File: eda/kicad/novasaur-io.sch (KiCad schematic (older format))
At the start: 72 parts, among them J1 POWER IN, J3 AUDIO OUT, J4 KEYBOARD, J5 SERIAL, J5 SPKR, J6 DISPLAY, J7 EXPANSION, J8 EXP OUT, J9 VIDEO, Q4 BS270, SW1 POWER, U1 74F86, U2 74F08, U38 CD4053, U39 MAX232, U4 74F32, U40 NJM4580, U41 MCP1827S, U6 74F139, U7 74F139

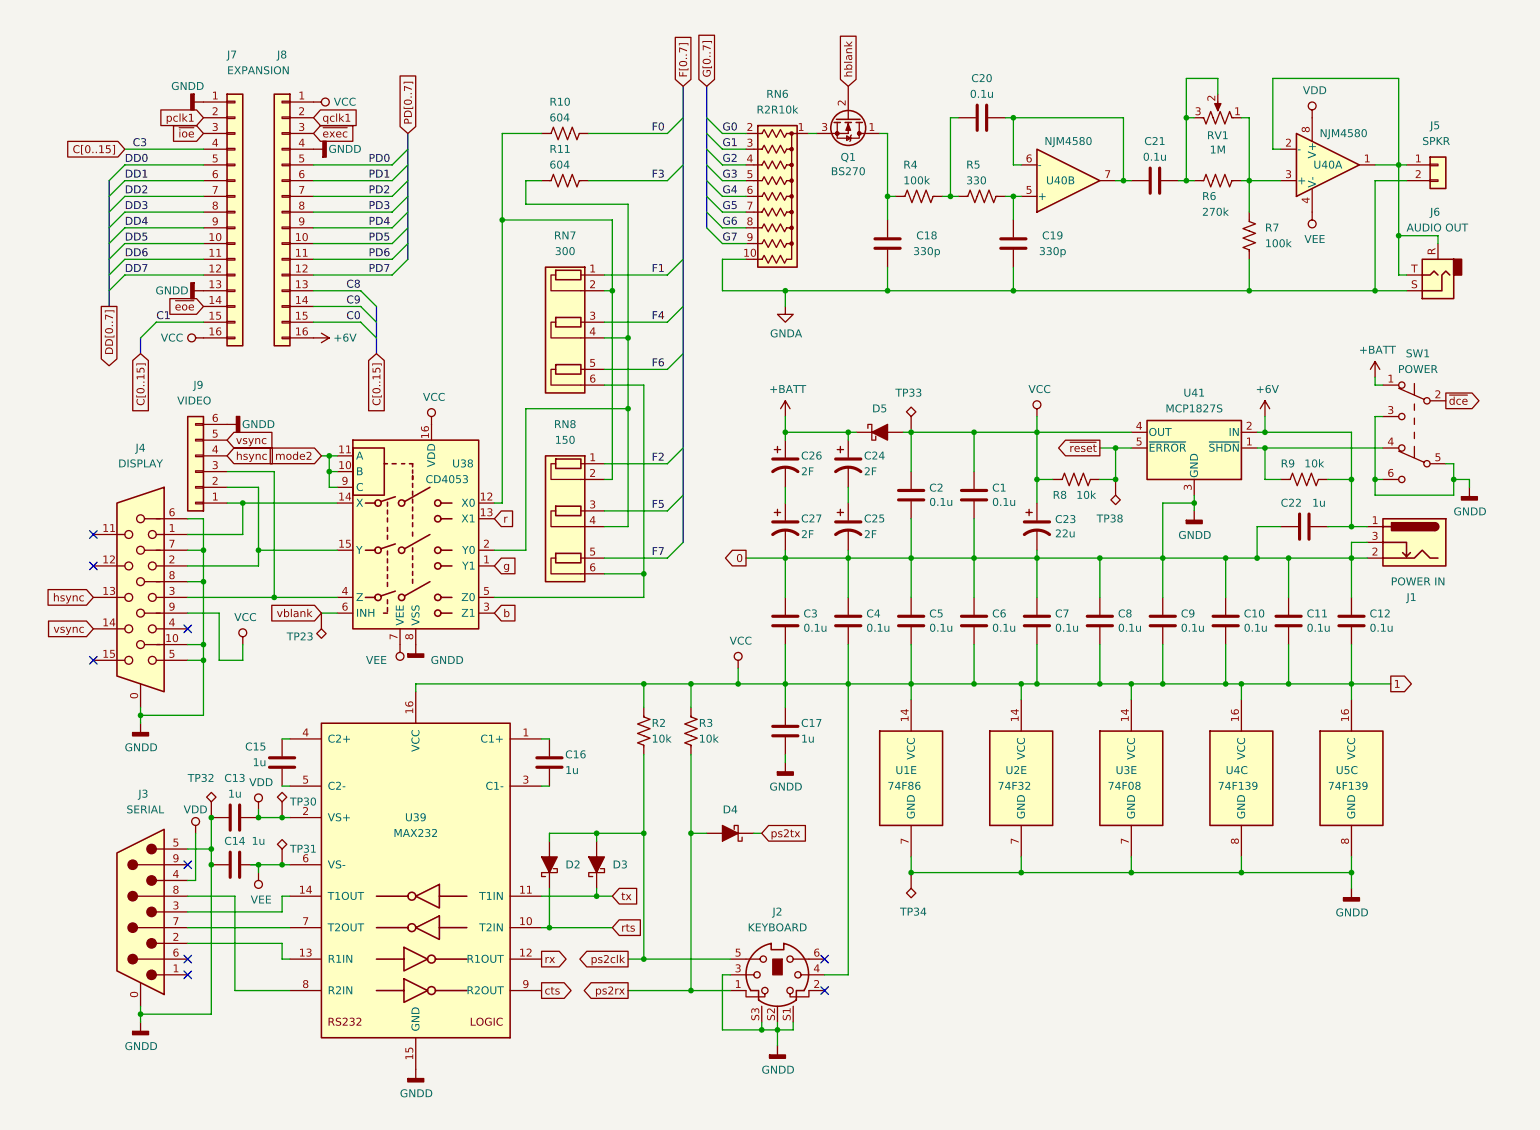
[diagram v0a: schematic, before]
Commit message: add dedicated ps2 clock enable line Use mode0|1 to select VDAC using DRL
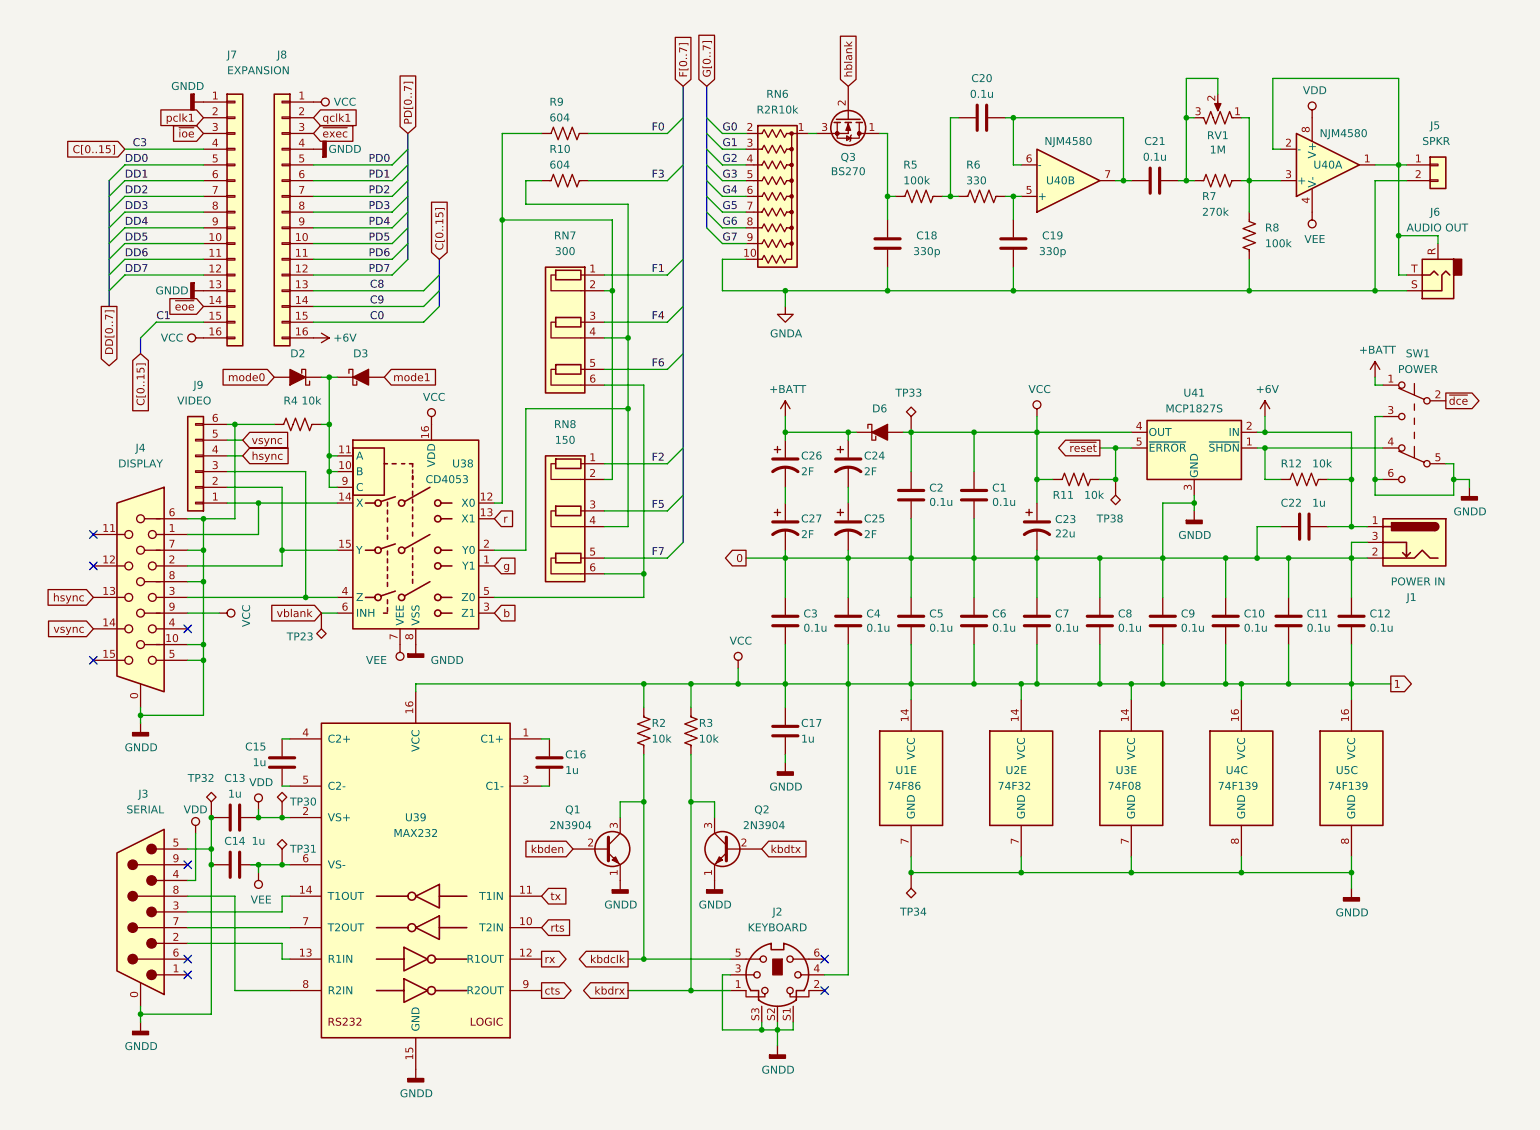
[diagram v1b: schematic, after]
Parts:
- removed D4: BAT42, Diode_THT:D_DO-35_SOD27_P7.62mm_Horizontal, symbol Device:D_Schottky_ALT
- added Q1, Q2: 2N3904, Package_TO_SOT_THT:TO-92_HandSolder, symbol Transistor_BJT:2N3904
- added R4: 10k, Resistor_THT:R_Axial_DIN0204_L3.6mm_D1.6mm_P7.62mm_Horizontal, symbol Device:R_US
- renumbered D5 to D6, R11 to R10, R8 to R11, R9 to R12, R4 to R5, R5 to R6, R6 to R7, R7 to R8, R10 to R9
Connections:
- net GNDD: now also Q1.1 (E), Q2.1 (E), R4.1
- net rts: no longer D2.1 (K)
- net tx: no longer D3.1 (K)
- net mode2: no longer names the net of U38.10 (B), U38.11 (A), U38.9 (C)
- net mode2: now also D2.1 (K), D3.1 (K), R4.2
- net ps2clk renamed kbdclk
- net kbdclk: now also Q1.3 (C); no longer D2.2 (A), D3.2 (A)
- net ps2rx renamed kbdrx
- net kbdrx: now also Q2.3 (C)
- new net kbden: Q1.2 (B)
- new net kbdtx: Q2.2 (B)
- new net mode0: D2.2 (A)
- new net mode1: D3.2 (A)

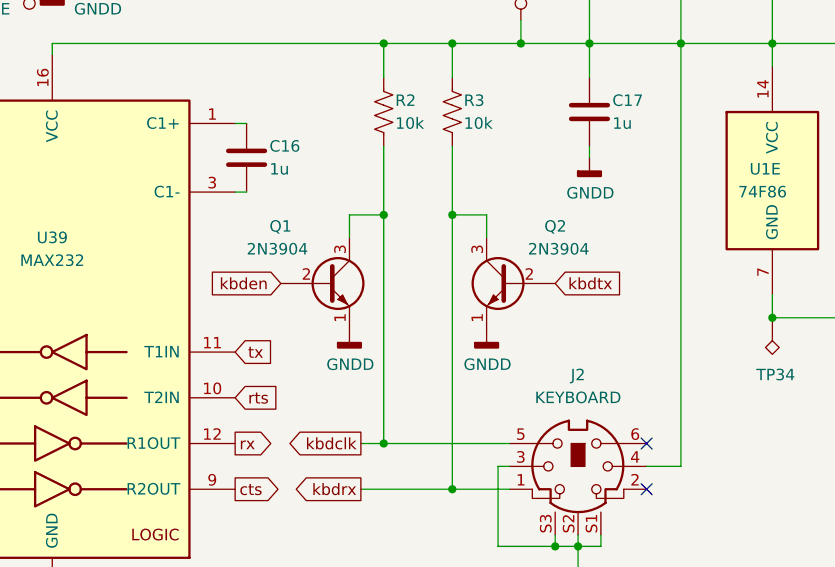
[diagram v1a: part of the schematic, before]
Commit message: refactor comms Add keyboard scan jump page, overload tx mode state to select keyboard jump page
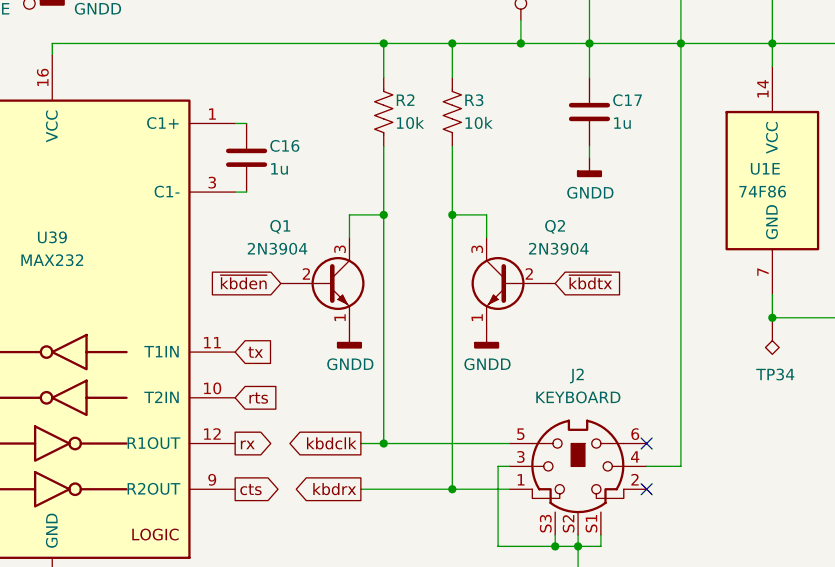
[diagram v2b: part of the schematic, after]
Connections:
- net kbden renamed ~kbden
- net kbdtx renamed ~kbdtx
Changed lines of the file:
@@
 	5300 7100 5400 7100
 Text GLabel 5300 5950 2    50   Input ~ 0
-kbdtx
+~kbdtx
 Connection ~ 5150 4900
 Connection ~ 5300 7100
@@
 $EndComp
 Text GLabel 4100 5950 0    50   Input ~ 0
-kbden
+~kbden
 $Comp
 L Device:R_US R?

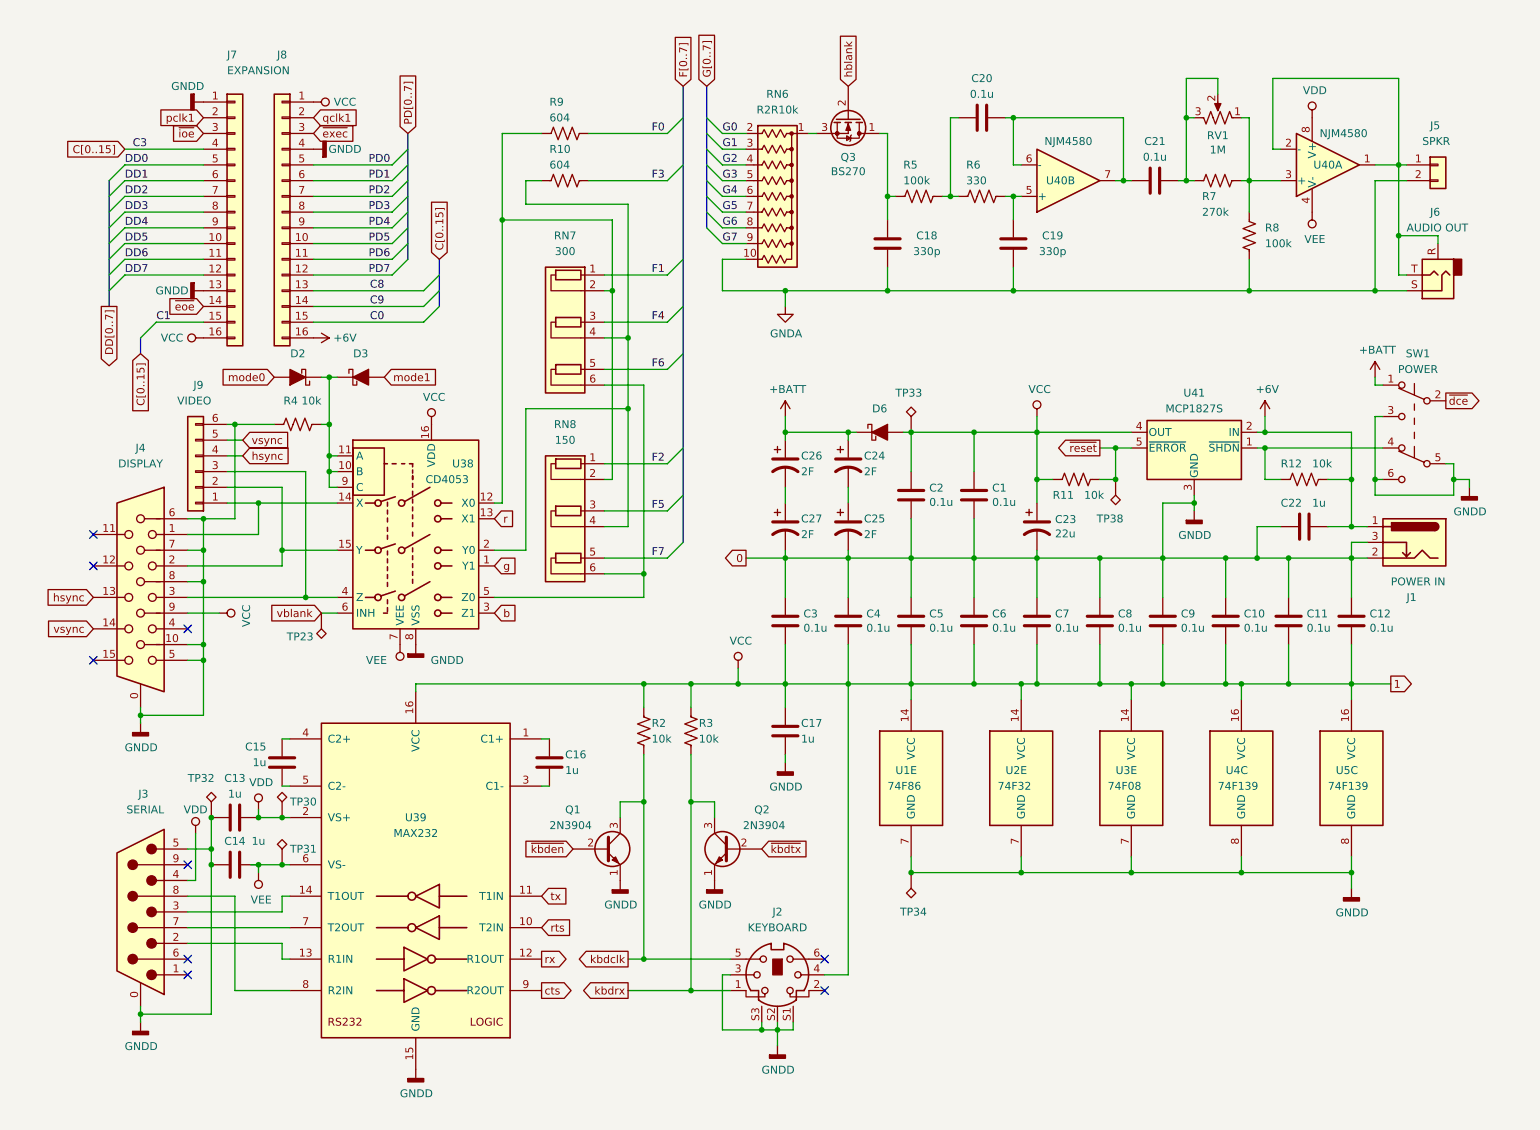
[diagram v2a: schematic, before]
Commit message: fix video timing debug and finish video modes
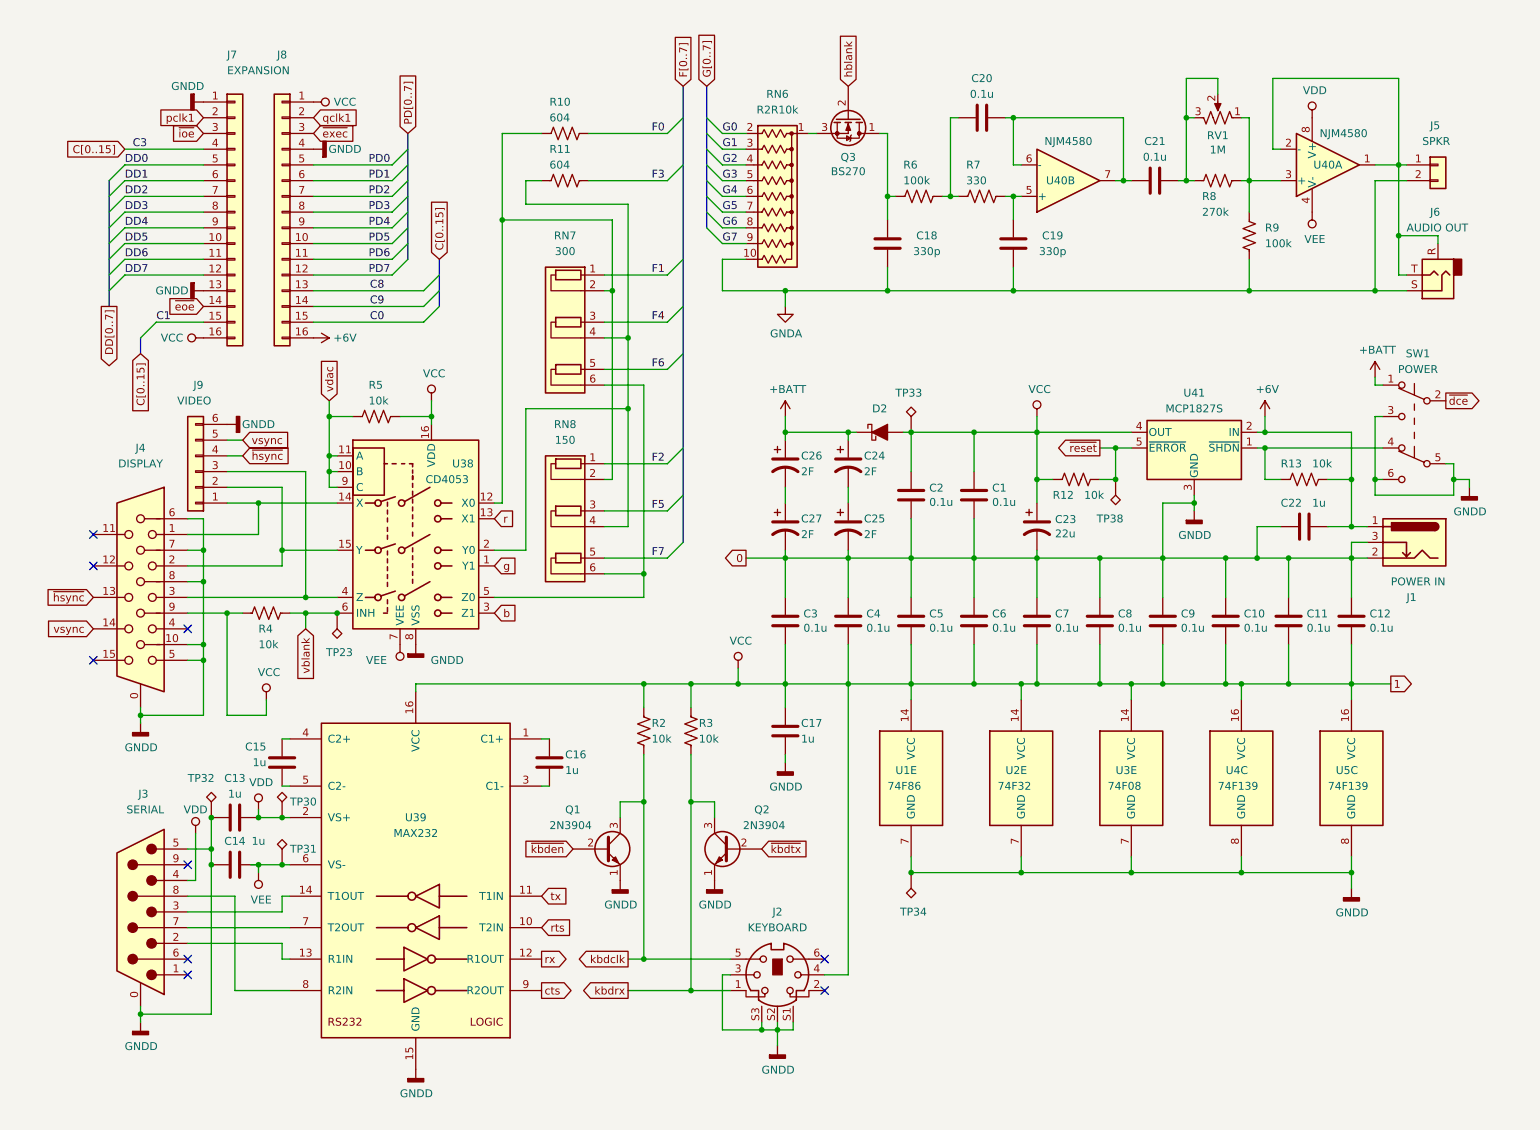
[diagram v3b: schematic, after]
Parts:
- removed D2, D3: BAT42, Diode_THT:D_DO-35_SOD27_P7.62mm_Horizontal, symbol Device:D_Schottky_ALT
- added R5: 10k, Resistor_THT:R_Axial_DIN0204_L3.6mm_D1.6mm_P7.62mm_Horizontal, symbol Device:R_US
- renumbered D6 to D2, R9 to R10, R10 to R11, R11 to R12, R12 to R13, R5 to R6, R6 to R7, R7 to R8, R8 to R9
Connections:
- net GNDD: no longer R4.1
- net VCC: now also R4.2, R5.1
- net vblank: now also R4.1
- net vdac: now reaches U38.10 (B), U38.11 (A), U38.9 (C)
- net vdac: now also R5.2; no longer R4.2
- net hsync renamed ~hsync
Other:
- moved on the sheet: TP23
